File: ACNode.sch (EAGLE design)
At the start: 41 parts, among them IC1 74AHC1G04DCK, U2 MAGJACK-POE, Y1 25mhz, Y2 20mhz

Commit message: Add 5v regulator and SL030 connector
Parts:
- added C17, C18: 10uf, SparkFun-Passives:CAP_POL1206
- added C19: 0.1uF, SparkFun-Passives:CAP0603-CAP
- added IC2: MC78M05CDTG, linear:MC78M05CDTG
- added LED1: (no value), SparkFun-LED:LED0603
- added R15: 200, SparkFun-Passives:RESISTOR0603-RES
- added SL030: (no value), pinhead:PINHD-1X6
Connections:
- new net N$26: LED1.A, R15.1
- new net RAW: C17.+, IC2.VI, U2.V+
- new net RFIN: SL030.2
- new net RFOUT: SL030.5
- net GND: now also C17.-, C18.-, C19.2, IC2.GND, LED1.C, SL030.6, U2.V-
- net SCL: now also SL030.4
- net SDA: now also SL030.3
- net VCC: now also C18.+, C19.1, IC2.VO, R15.2, SL030.1
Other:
- moved on the sheet: C14
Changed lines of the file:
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@@
 <part name="P+6" library="supply1" deviceset="VCC" device=""/>
 <part name="FDTI" library="pinhead" deviceset="PINHD-1X6" device=""/>
+<part name="SL030" library="pinhead" deviceset="PINHD-1X6" device=""/>
+<part name="IC2" library="linear" deviceset="MC78M" device="" technology="05CDTG"/>
+<part name="GND18" library="supply1" deviceset="GND" device=""/>
+<part name="C17" library="SparkFun-Passives" deviceset="CAP_POL" device="1206" value="10uf"/>
+<part name="GND19" library="supply1" deviceset="GND" device=""/>
+<part name="C18" library="SparkFun-Passives" deviceset="CAP_POL" device="1206" value="10uf"/>
+<part name="C19" library="SparkFun-Passives" deviceset="CAP" device="0603-CAP" value="0.1uF"/>
+<part name="GND20" library="supply1" deviceset="GND" device=""/>
+<part name="GND21" library="supply1" deviceset="GND" device=""/>
+<part name="R15" library="SparkFun-Passives" deviceset="RESISTOR" device="0603-RES" value="200"/>
+<part name="P+7" library="supply1" deviceset="VCC" device=""/>
+<part name="LED1" library="SparkFun-LED" deviceset="LED" device="0603"/>
+<part name="GND22" library="supply1" deviceset="GND" device=""/>
 </parts>
 <sheets>
@@
 <text x="165.1" y="25.4" size="3.81" layer="94" font="vector">Charles Yarnold</text>
 <text x="236.22" y="25.4" size="3.81" layer="94" font="vector">CC-BY-SA</text>
-<wire x1="154.94" y1="177.8" x2="154.94" y2="154.94" width="0.1524" layer="94"/>
-<wire x1="154.94" y1="154.94" x2="172.72" y2="154.94" width="0.1524" layer="94"/>
-<wire x1="172.72" y1="154.94" x2="172.72" y2="147.32" width="0.1524" layer="94"/>
-<wire x1="172.72" y1="147.32" x2="180.34" y2="147.32" width="0.1524" layer="94"/>
-<wire x1="180.34" y1="147.32" x2="180.34" y2="134.62" width="0.1524" layer="94"/>
-<wire x1="180.34" y1="134.62" x2="190.5" y2="134.62" width="0.1524" layer="94"/>
+<wire x1="165.1" y1="177.8" x2="165.1" y2="142.24" width="0.1524" layer="94"/>
 <wire x1="190.5" y1="134.62" x2="190.5" y2="116.84" width="0.1524" layer="94"/>
 <wire x1="190.5" y1="116.84" x2="200.66" y2="116.84" width="0.1524" layer="94"/>
-<wire x1="200.66" y1="116.84" x2="200.66" y2="91.44" width="0.1524" layer="94"/>
-<wire x1="200.66" y1="91.44" x2="261.62" y2="91.44" width="0.1524" layer="94"/>
-<wire x1="261.62" y1="91.44" x2="261.62" y2="177.8" width="0.1524" layer="94"/>
-<wire x1="261.62" y1="177.8" x2="154.94" y2="177.8" width="0.1524" layer="94"/>
+<wire x1="200.66" y1="116.84" x2="200.66" y2="93.98" width="0.1524" layer="94"/>
+<wire x1="200.66" y1="93.98" x2="261.62" y2="93.98" width="0.1524" layer="94"/>
+<wire x1="261.62" y1="93.98" x2="261.62" y2="177.8" width="0.1524" layer="94"/>
+<wire x1="261.62" y1="177.8" x2="165.1" y2="177.8" width="0.1524" layer="94"/>
 <wire x1="114.3" y1="73.66" x2="165.1" y2="73.66" width="0.1524" layer="94"/>
 <wire x1="165.1" y1="73.66" x2="165.1" y2="93.98" width="0.1524" layer="94"/>
-<wire x1="180.34" y1="134.62" x2="165.1" y2="134.62" width="0.1524" layer="94"/>
+<wire x1="190.5" y1="134.62" x2="165.1" y2="134.62" width="0.1524" layer="94"/>
 <wire x1="165.1" y1="116.84" x2="190.5" y2="116.84" width="0.1524" layer="94"/>
+<wire x1="200.66" y1="93.98" x2="165.1" y2="93.98" width="0.1524" layer="94"/>
+<wire x1="101.6" y1="177.8" x2="165.1" y2="177.8" width="0.1524" layer="94"/>
 </plain>
 <instances>
@@
 <instance part="P+3" gate="VCC" x="193.04" y="149.86" rot="R90"/>
 <instance part="R12" gate="G$1" x="190.5" y="165.1" rot="R90"/>
-<instance part="C14" gate="G$1" x="170.18" y="160.02" rot="R90"/>
+<instance part="C14" gate="G$1" x="172.72" y="157.48" rot="R180"/>
 <instance part="GND15" gate="1" x="182.88" y="172.72" rot="R180"/>
 <instance part="S1" gate="S" x="180.34" y="165.1" rot="R90"/>
@@
 <instance part="P+6" gate="VCC" x="259.08" y="129.54" rot="R180"/>
 <instance part="FDTI" gate="A" x="180.34" y="132.08" rot="R90"/>
+<instance part="SL030" gate="A" x="185.42" y="111.76" rot="R90"/>
+<instance part="IC2" gate="G$1" x="127" y="167.64"/>
+<instance part="GND18" gate="1" x="127" y="154.94"/>
+<instance part="C17" gate="G$1" x="111.76" y="165.1"/>
+<instance part="GND19" gate="1" x="111.76" y="154.94"/>
+<instance part="C18" gate="G$1" x="142.24" y="165.1"/>
+<instance part="C19" gate="G$1" x="152.4" y="162.56"/>
+<instance part="GND20" gate="1" x="142.24" y="154.94"/>
+<instance part="GND21" gate="1" x="152.4" y="154.94"/>
+<instance part="R15" gate="G$1" x="160.02" y="157.48" rot="R90"/>
+<instance part="P+7" gate="VCC" x="160.02" y="172.72"/>
+<instance part="LED1" gate="G$1" x="157.48" y="147.32" rot="R270"/>
+<instance part="GND22" gate="1" x="147.32" y="147.32" rot="R270"/>
 </instances>
 <busses>
@@
 <label x="185.42" y="119.38" size="1.778" layer="95" rot="R90"/>
 </segment>
+<segment>
+<pinref part="SL030" gate="A" pin="6"/>
+<wire x1="190.5" y1="109.22" x2="190.5" y2="96.52" width="0.1524" layer="91"/>
+<label x="190.5" y="96.52" size="1.778" layer="95" rot="R90"/>
+</segment>
+<segment>
+<pinref part="U2" gate="G$1" pin="V-"/>
+<wire x1="106.68" y1="129.54" x2="99.06" y2="129.54" width="0.1524" layer="91"/>
+<label x="99.06" y="129.54" size="1.778" layer="95"/>
+</segment>
+<segment>
+<pinref part="IC2" gate="G$1" pin="GND"/>
+<pinref part="GND18" gate="1" pin="GND"/>
+<wire x1="127" y1="160.02" x2="127" y2="157.48" width="0.1524" layer="91"/>
+</segment>
+<segment>
+<pinref part="C17" gate="G$1" pin="-"/>
+<pinref part="GND19" gate="1" pin="GND"/>
+<wire x1="111.76" y1="160.02" x2="111.76" y2="157.48" width="0.1524" layer="91"/>
+</segment>
+<segment>
+<pinref part="C18" gate="G$1" pin="-"/>
+<pinref part="GND20" gate="1" pin="GND"/>
+<wire x1="142.24" y1="160.02" x2="142.24" y2="157.48" width="0.1524" layer="91"/>
+</segment>
+<segment>
+<pinref part="C19" gate="G$1" pin="2"/>
+<pinref part="GND21" gate="1" pin="GND"/>
+<wire x1="152.4" y1="160.02" x2="152.4" y2="157.48" width="0.1524" layer="91"/>
+</segment>
+<segment>
+<pinref part="GND22" gate="1" pin="GND"/>
+<pinref part="LED1" gate="G$1" pin="C"/>
+<wire x1="149.86" y1="147.32" x2="152.4" y2="147.32" width="0.1524" layer="91"/>
+</segment>
 </net>
 <net name="N$6" class="0">
@@
 <label x="180.34" y="119.38" size="1.778" layer="95" rot="R90"/>
 </segment>
+<segment>
+<pinref part="SL030" gate="A" pin="1"/>
+<wire x1="177.8" y1="109.22" x2="177.8" y2="96.52" width="0.1524" layer="91"/>
+<label x="177.8" y="96.52" size="1.778" layer="95" rot="R90"/>
+</segment>
+<segment>
+<pinref part="IC2" gate="G$1" pin="VO"/>
+<pinref part="C18" gate="G$1" pin="+"/>
+<wire x1="137.16" y1="167.64" x2="142.24" y2="167.64" width="0.1524" layer="91"/>
+<pinref part="C19" gate="G$1" pin="1"/>
+<wire x1="142.24" y1="167.64" x2="152.4" y2="167.64" width="0.1524" layer="91"/>
+<pinref part="R15" gate="G$1" pin="2"/>
+<wire x1="152.4" y1="167.64" x2="160.02" y2="167.64" width="0.1524" layer="91"/>
+<wire x1="160.02" y1="167.64" x2="160.02" y2="162.56" width="0.1524" layer="91"/>
+<pinref part="P+7" gate="VCC" pin="VCC"/>
+<wire x1="160.02" y1="167.64" x2="160.02" y2="170.18" width="0.1524" layer="91"/>
+</segment>
 </net>
 <net name="N$23" class="0">
@@
 <segment>
 <pinref part="C14" gate="G$1" pin="1"/>
-<wire x1="165.1" y1="160.02" x2="157.48" y2="160.02" width="0.1524" layer="91"/>
-<label x="157.48" y="160.02" size="1.778" layer="95" font="vector"/>
+<wire x1="172.72" y1="152.4" x2="172.72" y2="147.32" width="0.1524" layer="91"/>
+<label x="172.72" y="147.32" size="1.778" layer="95" font="vector" rot="R90"/>
 </segment>
 <segment>
@@
 <label x="154.94" y="81.28" size="1.778" layer="95"/>
 </segment>
+<segment>
+<pinref part="SL030" gate="A" pin="3"/>
+<wire x1="182.88" y1="109.22" x2="182.88" y2="96.52" width="0.1524" layer="91"/>
+<label x="182.88" y="96.52" size="1.778" layer="95" rot="R90"/>
+</segment>
 </net>
 <net name="SCL" class="0">
@@
 <label x="154.94" y="83.82" size="1.778" layer="95"/>
 </segment>
+<segment>
+<pinref part="SL030" gate="A" pin="4"/>
+<wire x1="185.42" y1="109.22" x2="185.42" y2="96.52" width="0.1524" layer="91"/>
+<label x="185.42" y="96.52" size="1.778" layer="95" rot="R90"/>
+</segment>
 </net>
 <net name="TXO" class="0">
@@
 </segment>
 </net>
+<net name="RFIN" class="0">
+<segment>
+<pinref part="SL030" gate="A" pin="2"/>
+<wire x1="180.34" y1="109.22" x2="180.34" y2="96.52" width="0.1524" layer="91"/>
+<label x="180.34" y="96.52" size="1.778" layer="95" rot="R90"/>
+</segment>
+</net>
+<net name="RFOUT" class="0">
+<segment>
+<pinref part="SL030" gate="A" pin="5"/>
+<wire x1="187.96" y1="109.22" x2="187.96" y2="96.52" width="0.1524" layer="91"/>
+<label x="187.96" y="96.52" size="1.778" layer="95" rot="R90"/>
+</segment>
+</net>
+<net name="RAW" class="0">
+<segment>
+<pinref part="U2" gate="G$1" pin="V+"/>
+<wire x1="106.68" y1="132.08" x2="99.06" y2="132.08" width="0.1524" layer="91"/>
+<label x="99.06" y="132.08" size="1.778" layer="95"/>
+</segment>
+<segment>
+<pinref part="IC2" gate="G$1" pin="VI"/>
+<wire x1="116.84" y1="167.64" x2="111.76" y2="167.64" width="0.1524" layer="91"/>
+<pinref part="C17" gate="G$1" pin="+"/>
+<wire x1="111.76" y1="167.64" x2="106.68" y2="167.64" width="0.1524" layer="91"/>
+<label x="106.68" y="167.64" size="1.778" layer="95"/>
+</segment>
+</net>
+<net name="N$26" class="0">
+<segment>
+<pinref part="R15" gate="G$1" pin="1"/>
+<pinref part="LED1" gate="G$1" pin="A"/>
+<wire x1="160.02" y1="152.4" x2="160.02" y2="147.32" width="0.1524" layer="91"/>
+</segment>
+</net>

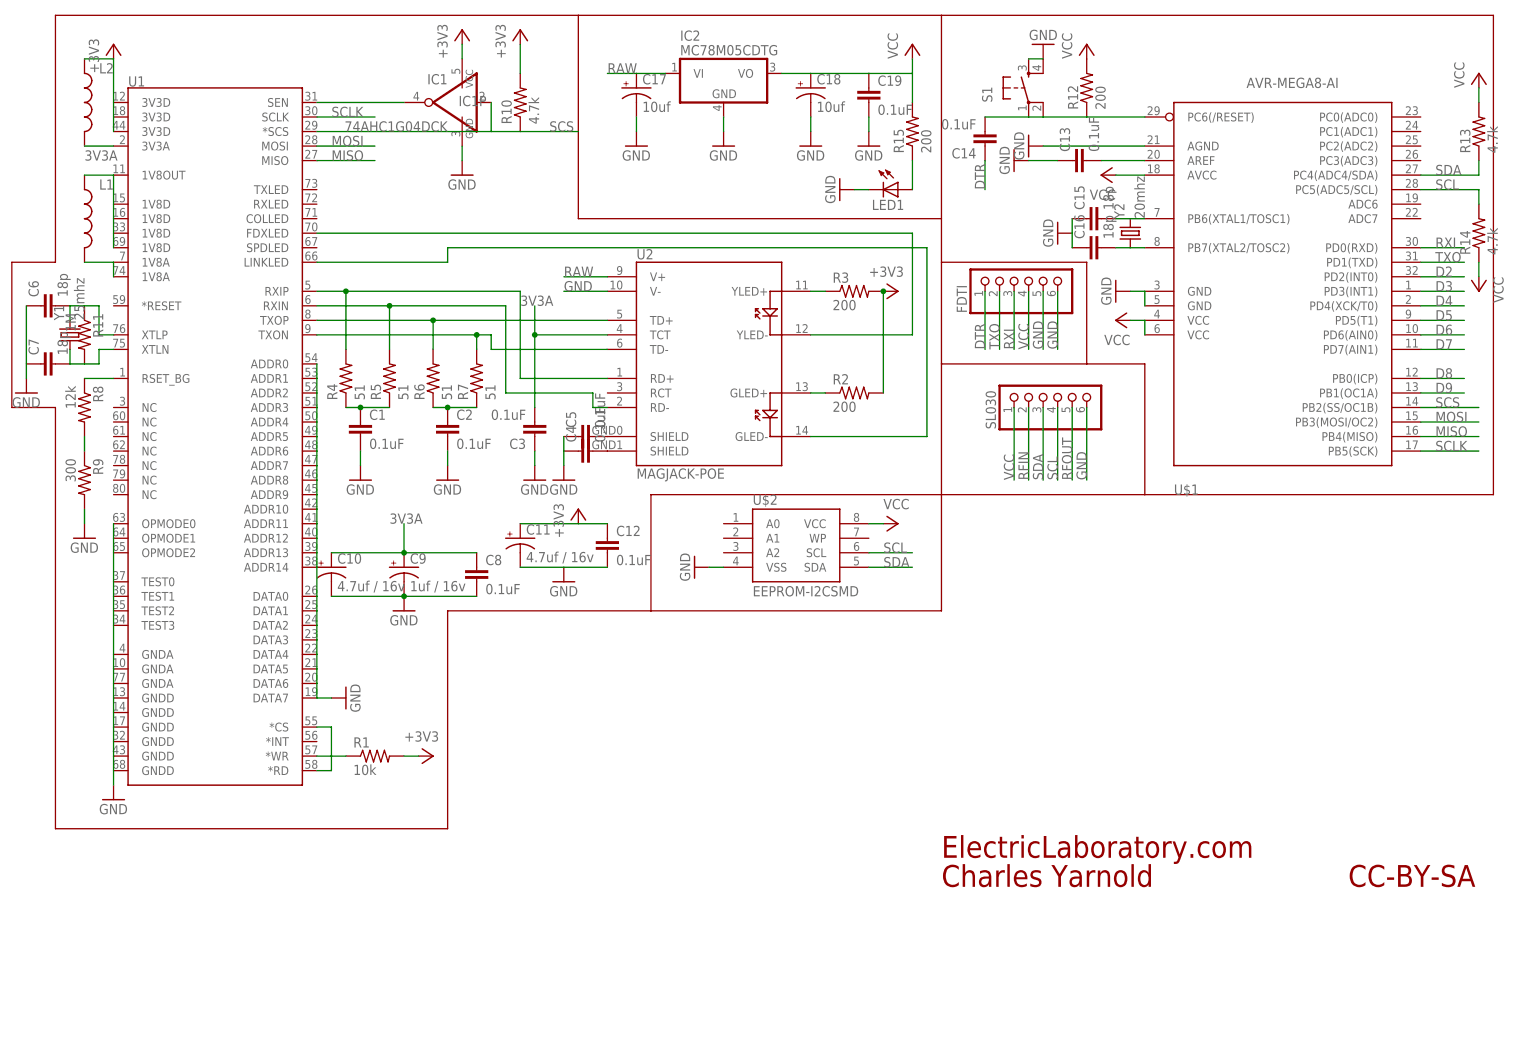
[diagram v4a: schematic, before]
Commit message: Label those schematics
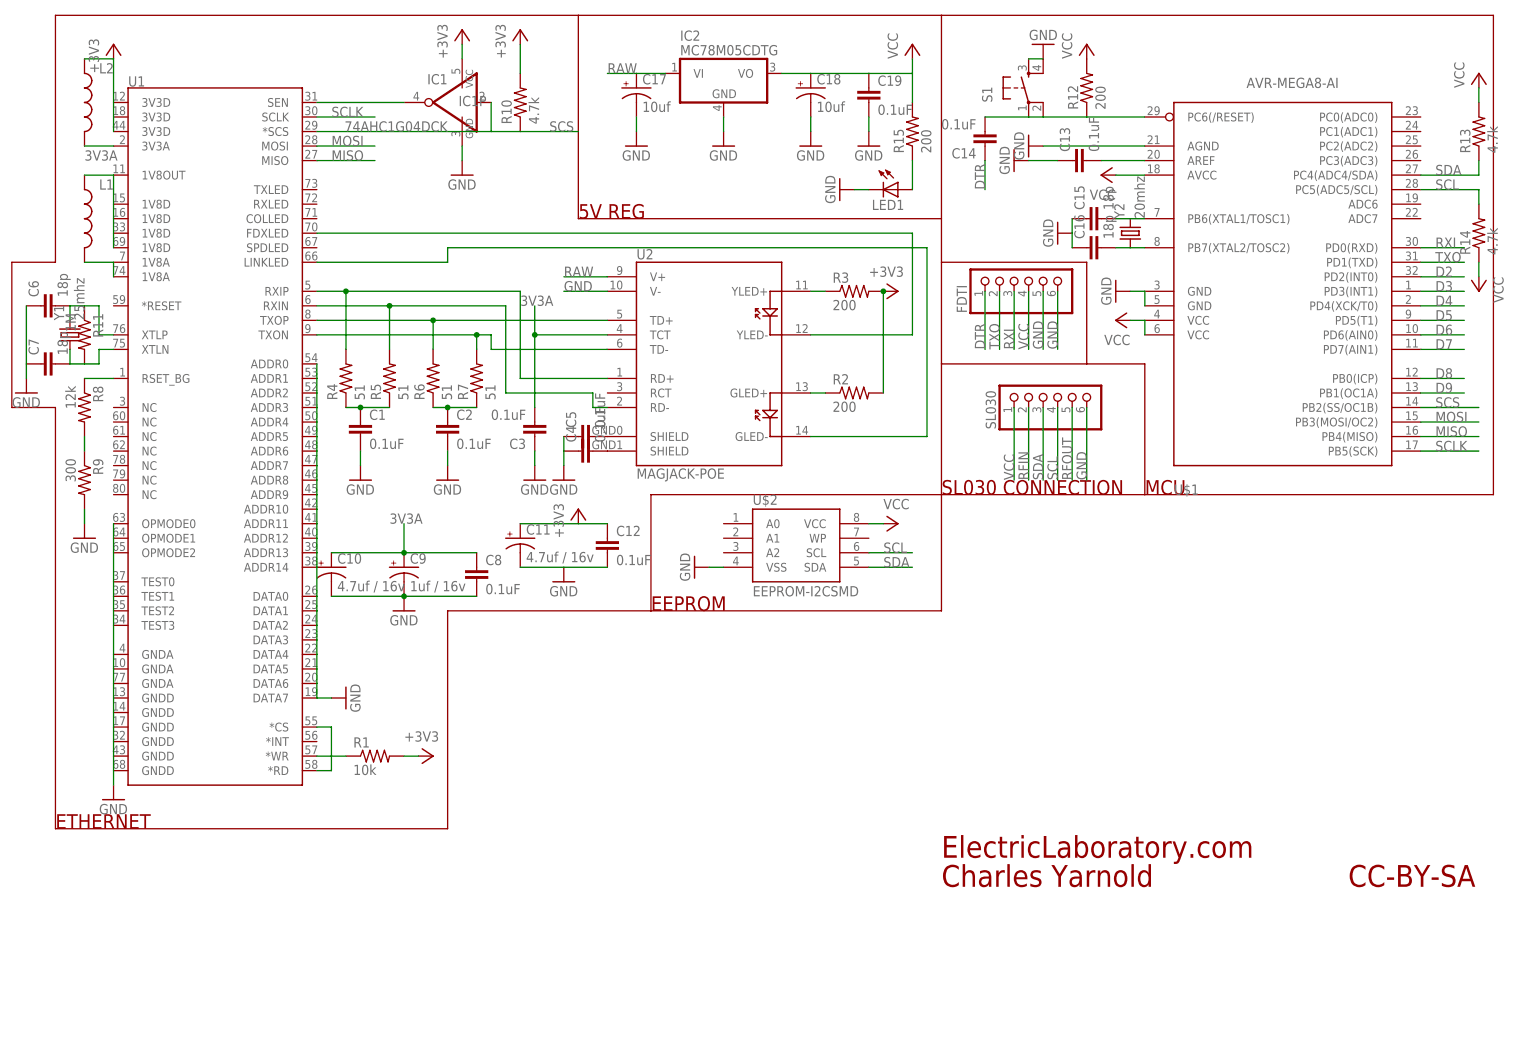
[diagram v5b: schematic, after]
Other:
- note added: "5V REG"
- note added: "EEPROM"
- note added: "ETHERNET"
- note added: "MCU"
- note added: "SL030 CONNECTION"
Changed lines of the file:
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@@
 <wire x1="200.66" y1="93.98" x2="165.1" y2="93.98" width="0.1524" layer="94"/>
 <wire x1="101.6" y1="177.8" x2="165.1" y2="177.8" width="0.1524" layer="94"/>
+<text x="10.16" y="35.56" size="2.54" layer="94">ETHERNET</text>
+<text x="200.66" y="93.98" size="2.54" layer="94">MCU</text>
+<text x="101.6" y="142.24" size="2.54" layer="94">5V REG</text>
+<text x="114.3" y="73.66" size="2.54" layer="94">EEPROM</text>
+<text x="165.1" y="93.98" size="2.54" layer="94">SL030 CONNECTION</text>
 </plain>
 <instances>

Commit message: Add 3v3 reg and voltage out
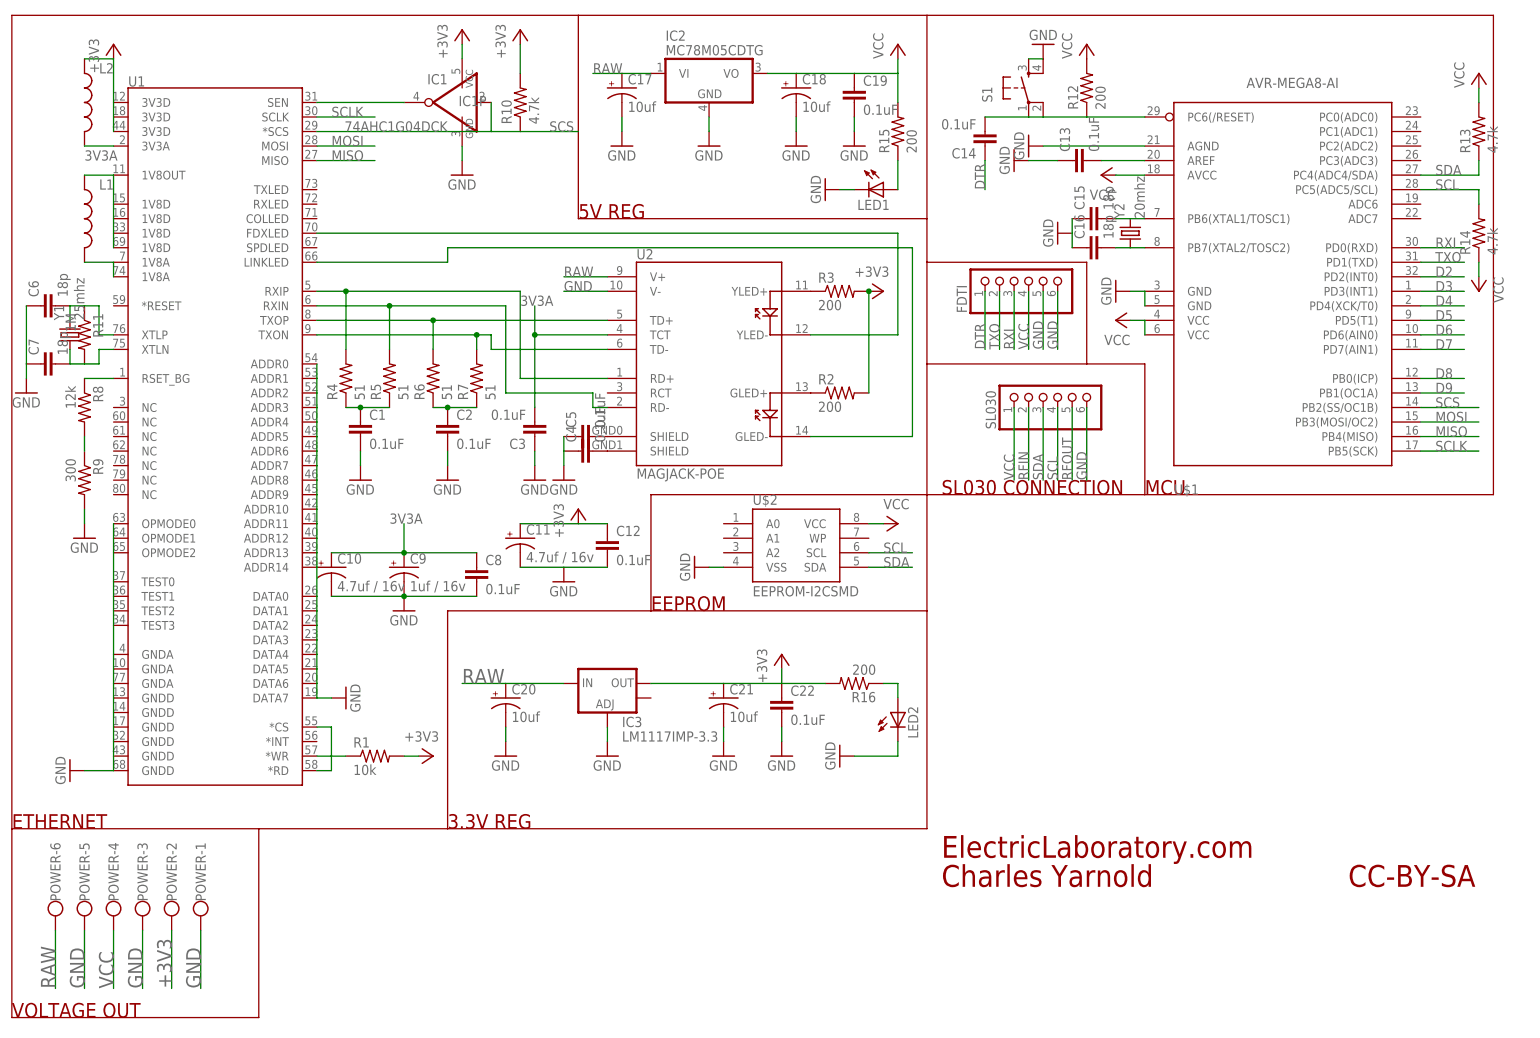
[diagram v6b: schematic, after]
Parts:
- added C20, C21: 10uf, SparkFun-Passives:CAP_POL1206
- added C22: 0.1uF, SparkFun-Passives:CAP0603-CAP
- added IC3: LM1117IMP-3.3, SparkFun-PowerIC:V_REG_LM1117SOT223
- added LED2: (no value), SparkFun-LED:LED0603
- added POWER: (no value), con-wago-500:W237-6
- added R16: 200, SparkFun-Passives:RESISTOR0805-RES
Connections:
- new net N$28: LED2.A, R16.1
- net +3V3: now also C21.+, C22.1, IC3.OUT, POWER-2.KL, R16.2
- net GND: now also C20.-, C21.-, C22.2, IC3.ADJ, LED2.C, POWER-1.KL, POWER-3.KL, POWER-5.KL
- net RAW: now also C20.+, IC3.IN, POWER-6.KL
- net VCC: now also POWER-4.KL
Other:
- note added: "3.3V REG"
- note added: "VOLTAGE OUT"
- moved on the sheet: C17, C18, C19, IC2, LED1, R15, R2, R3
